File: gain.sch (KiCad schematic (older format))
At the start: 15 parts

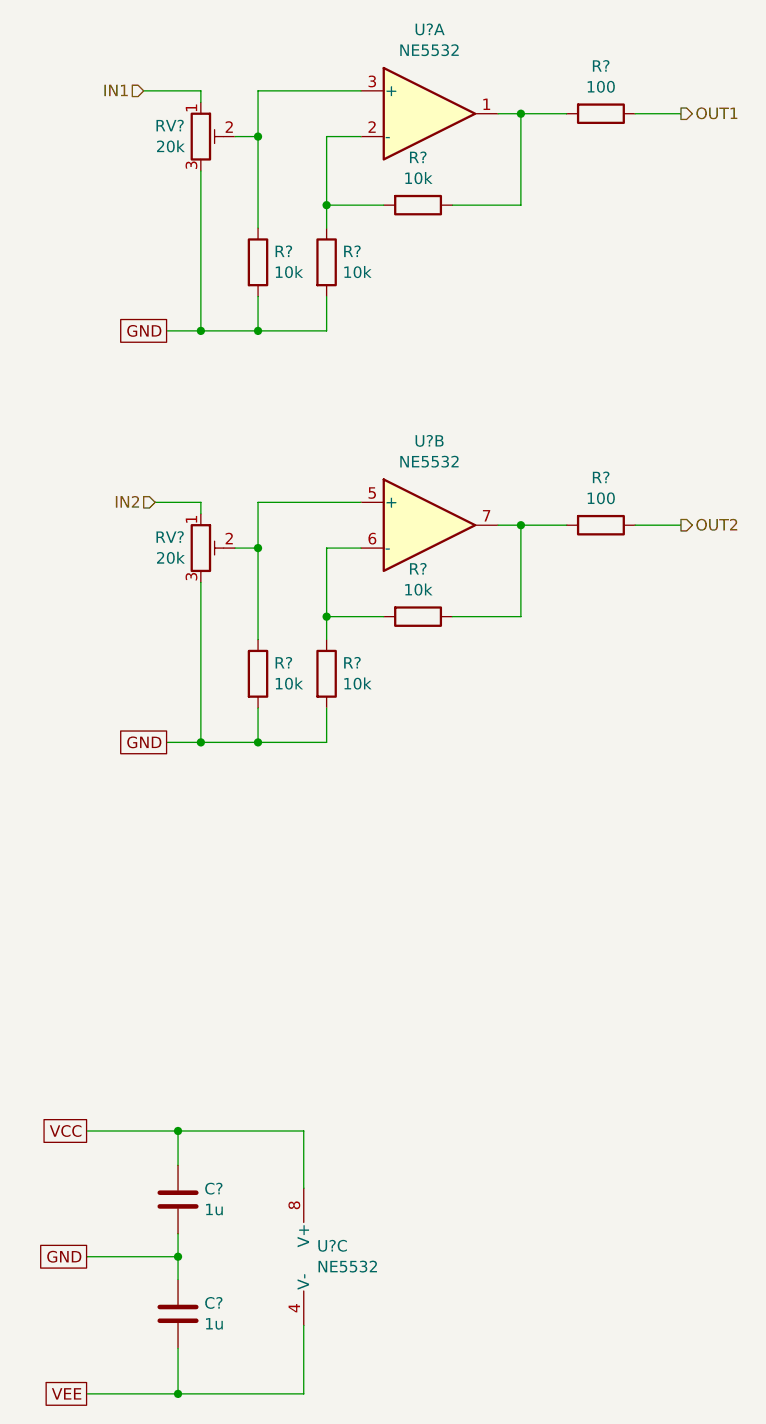
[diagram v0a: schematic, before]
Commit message: improved PSU, gain up front, reordered filter stages, shrunk rumble filter
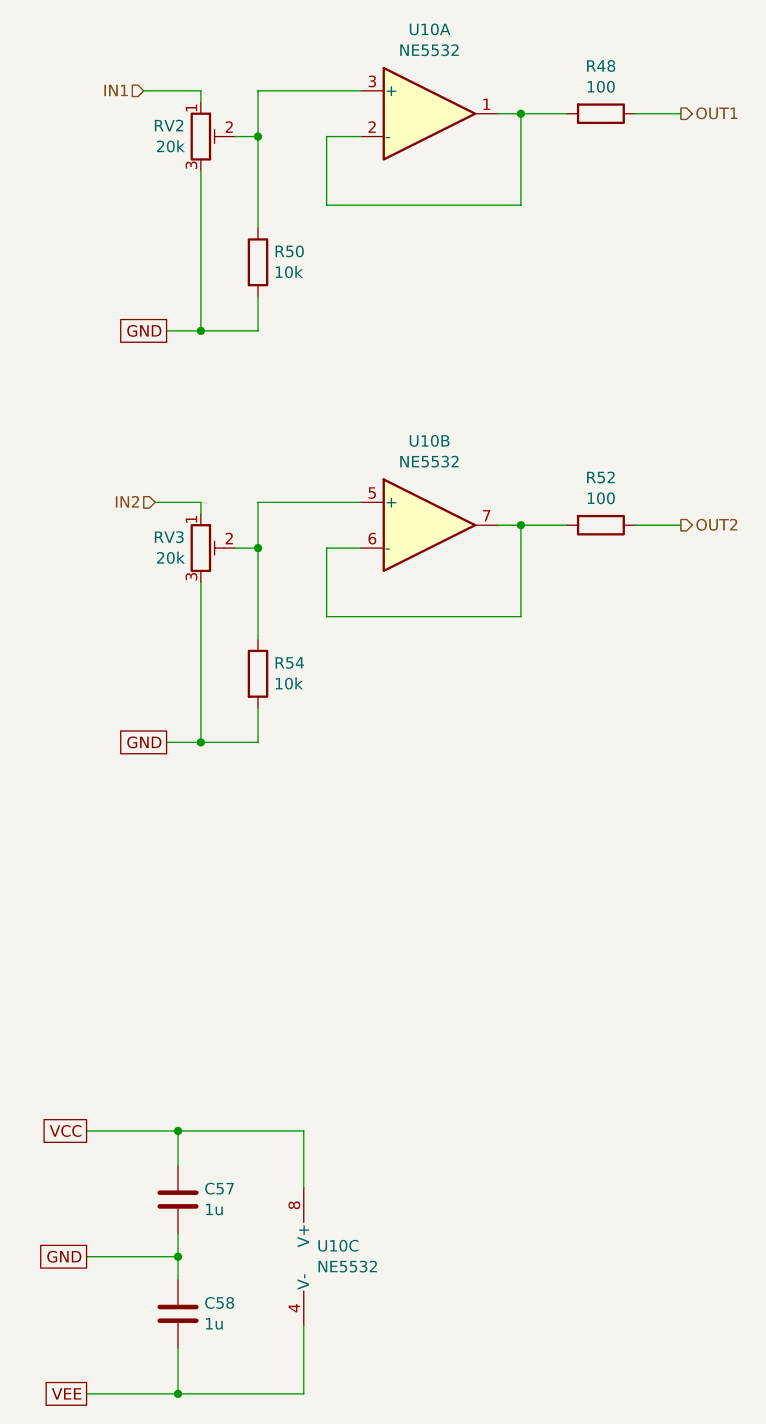
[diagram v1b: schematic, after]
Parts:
- removed R? (x4): 10k, Resistors_SMD:R_0805, symbol Device:R
- gave numbers to parts that had none: 9
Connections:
- net at R56.2, U11.1: now also U11.2 (-)
- net at U11.6 (-): now also R60.2, U11.7
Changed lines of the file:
@@
 $Descr A4 11693 8268
 encoding utf-8
-Sheet 11 13
+Sheet 13 13
 Title "Output Gain Controls"
 Date "2021-10-03"
@@
 AR Path="/61597701/61606DFA" Ref="U?"  Part="3"
 AR Path="/615C4B54/61606DFA" Ref="U?"  Part="3"
-AR Path="/61604458/61606DFA" Ref="U?"  Part="3"
-AR Path="/6164D7C0/61606DFA" Ref="U?"  Part="3"
+AR Path="/61604458/61606DFA" Ref="U11"  Part="3"
+AR Path="/6164D7C0/61606DFA" Ref="U10"  Part="3"
 AR Path="/61651AA2/61606DFA" Ref="U?"  Part="3"
-F 0 "U?" H 2808 6846 50  0000 L CNN
+F 0 "U10" H 2808 6846 50  0000 L CNN
 F 1 "NE5532" H 2808 6755 50  0000 L CNN
 F 2 "Housings_DIP:DIP-8_W7.62mm_Socket" H 2850 6800 50  0001 C CNN
@@
 AR Path="/61597701/61606E00" Ref="C?"  Part="1"
 AR Path="/615C4B54/61606E00" Ref="C?"  Part="1"
-AR Path="/61604458/61606E00" Ref="C?"  Part="1"
-AR Path="/6164D7C0/61606E00" Ref="C?"  Part="1"
+AR Path="/61604458/61606E00" Ref="C60"  Part="1"
+AR Path="/6164D7C0/61606E00" Ref="C58"  Part="1"
 AR Path="/61651AA2/61606E00" Ref="C?"  Part="1"
-F 0 "C?" H 2315 7096 50  0000 L CNN
+F 0 "C58" H 2315 7096 50  0000 L CNN
 F 1 "1u" H 2315 7005 50  0000 L CNN
 F 2 "Capacitors_SMD:C_0805" H 2238 6900 50  0001 C CNN
@@
 AR Path="/61597701/61606E06" Ref="C?"  Part="1"
 AR Path="/615C4B54/61606E06" Ref="C?"  Part="1"
-AR Path="/61604458/61606E06" Ref="C?"  Part="1"
-AR Path="/6164D7C0/61606E06" Ref="C?"  Part="1"
+AR Path="/61604458/61606E06" Ref="C59"  Part="1"
+AR Path="/6164D7C0/61606E06" Ref="C57"  Part="1"
 AR Path="/61651AA2/61606E06" Ref="C?"  Part="1"
-F 0 "C?" H 2315 6596 50  0000 L CNN
+F 0 "C57" H 2315 6596 50  0000 L CNN
 F 1 "1u" H 2315 6505 50  0000 L CNN
 F 2 "Capacitors_SMD:C_0805" H 2238 6400 50  0001 C CNN
@@
 Connection ~ 2200 7400
 $Comp
-L Amplifier_Operational:NE5532 U?
+L Amplifier_Operational:NE5532 U11
 U 1 1 6160713F
 P 3300 1800
-AR Path="/61604458/6160713F" Ref="U?"  Part="1"
-AR Path="/6164D7C0/6160713F" Ref="U?"  Part="1"
+AR Path="/61604458/6160713F" Ref="U11"  Part="1"
+AR Path="/6164D7C0/6160713F" Ref="U10"  Part="1"
 AR Path="/61651AA2/6160713F" Ref="U?"  Part="1"
-F 0 "U?" H 3300 2167 50  0000 C CNN
+F 0 "U10" H 3300 2167 50  0000 C CNN
 F 1 "NE5532" H 3300 2076 50  0000 C CNN
 F 2 "" H 3300 1800 50  0001 C CNN
@@
 $EndComp
 $Comp
-L Amplifier_Operational:NE5532 U?
+L Amplifier_Operational:NE5532 U11
 U 2 1 61607B4F
 P 3300 3600
-AR Path="/61604458/61607B4F" Ref="U?"  Part="2"
-AR Path="/6164D7C0/61607B4F" Ref="U?"  Part="2"
+AR Path="/61604458/61607B4F" Ref="U11"  Part="2"
+AR Path="/6164D7C0/61607B4F" Ref="U10"  Part="2"
 AR Path="/61651AA2/61607B4F" Ref="U?"  Part="2"
-F 0 "U?" H 3300 3967 50  0000 C CNN
+F 0 "U10" H 3300 3967 50  0000 C CNN
 F 1 "NE5532" H 3300 3876 50  0000 C CNN
 F 2 "" H 3300 3600 50  0001 C CNN
@@
 $EndComp
 $Comp
-L Device:R_POT_TRIM RV?
+L Device:R_POT_TRIM RV4
 U 1 1 6160B080
 P 2300 1900
-AR Path="/61604458/6160B080" Ref="RV?"  Part="1"
-AR Path="/6164D7C0/6160B080" Ref="RV?"  Part="1"
+AR Path="/61604458/6160B080" Ref="RV4"  Part="1"
+AR Path="/6164D7C0/6160B080" Ref="RV2"  Part="1"
 AR Path="/61651AA2/6160B080" Ref="RV?"  Part="1"
-F 0 "RV?" H 2230 1946 50  0000 R CNN
+F 0 "RV2" H 2230 1946 50  0000 R CNN
 F 1 "20k" H 2230 1855 50  0000 R CNN
 F 2 "Potentiometers:Potentiometer_Trimmer_Bourns_3296W" H 2300 1900 50  0001 C CNN
@@
 $EndComp
 $Comp
-L Device:R R?
+L Device:R R58
 U 1 1 6160B89B
 P 2550 2450
-AR Path="/61604458/6160B89B" Ref="R?"  Part="1"
-AR Path="/6164D7C0/6160B89B" Ref="R?"  Part="1"
+AR Path="/61604458/6160B89B" Ref="R58"  Part="1"
+AR Path="/6164D7C0/6160B89B" Ref="R50"  Part="1"
 AR Path="/61651AA2/6160B89B" Ref="R?"  Part="1"
-F 0 "R?" H 2620 2496 50  0000 L CNN
+F 0 "R50" H 2620 2496 50  0000 L CNN
 F 1 "10k" H 2620 2405 50  0000 L CNN
 F 2 "Resistors_SMD:R_0805" V 2480 2450 50  0001 C CNN
@@
 	1    0    0    -1
 $EndComp
-$Comp
-L Device:R R?
-U 1 1 6160BF26
-P 2850 2450
-AR Path="/61604458/6160BF26" Ref="R?"  Part="1"
-AR Path="/6164D7C0/6160BF26" Ref="R?"  Part="1"
-AR Path="/61651AA2/6160BF26" Ref="R?"  Part="1"
-F 0 "R?" H 2920 2496 50  0000 L CNN
-F 1 "10k" H 2920 2405 50  0000 L CNN
-F 2 "Resistors_SMD:R_0805" V 2780 2450 50  0001 C CNN
-F 3 "~" H 2850 2450 50  0001 C CNN
-	1    2850 2450
-	1    0    0    -1
-$EndComp
-$Comp
-L Device:R R?
-U 1 1 6160C516
-P 3250 2200
-AR Path="/61604458/6160C516" Ref="R?"  Part="1"
-AR Path="/6164D7C0/6160C516" Ref="R?"  Part="1"
-AR Path="/61651AA2/6160C516" Ref="R?"  Part="1"
-F 0 "R?" V 3043 2200 50  0000 C CNN
-F 1 "10k" V 3134 2200 50  0000 C CNN
-F 2 "Resistors_SMD:R_0805" V 3180 2200 50  0001 C CNN
-F 3 "~" H 3250 2200 50  0001 C CNN
-	1    3250 2200
-	0    1    1    0
-$EndComp
 Wire Wire Line
 	2450 1900 2550 1900
@@
 	3000 1900 2850 1900
 Wire Wire Line
-	2850 1900 2850 2200
-Wire Wire Line
-	2850 2200 3100 2200
-Connection ~ 2850 2200
-Wire Wire Line
-	2850 2200 2850 2300
-Wire Wire Line
 	2550 1900 2550 2300
 Wire Wire Line
@@
 	2300 2750 2550 2750
 Wire Wire Line
-	2850 2750 2850 2600
-Wire Wire Line
 	2550 2600 2550 2750
-Wire Wire Line
-	2850 2750 2550 2750
-Connection ~ 2550 2750
 Wire Wire Line
 	2550 1700 3000 1700
@@
 	2300 1700 2300 1750
 $Comp
-L Device:R_POT_TRIM RV?
+L Device:R_POT_TRIM RV5
 U 1 1 61627D7A
 P 2300 3700
-AR Path="/61604458/61627D7A" Ref="RV?"  Part="1"
-AR Path="/6164D7C0/61627D7A" Ref="RV?"  Part="1"
+AR Path="/61604458/61627D7A" Ref="RV5"  Part="1"
+AR Path="/6164D7C0/61627D7A" Ref="RV3"  Part="1"
 AR Path="/61651AA2/61627D7A" Ref="RV?"  Part="1"
-F 0 "RV?" H 2230 3746 50  0000 R CNN
+F 0 "RV3" H 2230 3746 50  0000 R CNN
 F 1 "20k" H 2230 3655 50  0000 R CNN
 F 2 "Potentiometers:Potentiometer_Trimmer_Bourns_3296W" H 2300 3700 50  0001 C CNN
@@
 $EndComp
 $Comp
-L Device:R R?
+L Device:R R62
 U 1 1 61627D80
 P 2550 4250
-AR Path="/61604458/61627D80" Ref="R?"  Part="1"
-AR Path="/6164D7C0/61627D80" Ref="R?"  Part="1"
+AR Path="/61604458/61627D80" Ref="R62"  Part="1"
+AR Path="/6164D7C0/61627D80" Ref="R54"  Part="1"
 AR Path="/61651AA2/61627D80" Ref="R?"  Part="1"
-F 0 "R?" H 2620 4296 50  0000 L CNN
+F 0 "R54" H 2620 4296 50  0000 L CNN
 F 1 "10k" H 2620 4205 50  0000 L CNN
 F 2 "Resistors_SMD:R_0805" V 2480 4250 50  0001 C CNN
@@
 	1    0    0    -1
 $EndComp
-$Comp
-L Device:R R?
-U 1 1 61627D86
-P 2850 4250
-AR Path="/61604458/61627D86" Ref="R?"  Part="1"
-AR Path="/6164D7C0/61627D86" Ref="R?"  Part="1"
-AR Path="/61651AA2/61627D86" Ref="R?"  Part="1"
-F 0 "R?" H 2920 4296 50  0000 L CNN
-F 1 "10k" H 2920 4205 50  0000 L CNN
-F 2 "Resistors_SMD:R_0805" V 2780 4250 50  0001 C CNN
-F 3 "~" H 2850 4250 50  0001 C CNN
-	1    2850 4250
-	1    0    0    -1
-$EndComp
-$Comp
-L Device:R R?
-U 1 1 61627D8C
-P 3250 4000
-AR Path="/61604458/61627D8C" Ref="R?"  Part="1"
-AR Path="/6164D7C0/61627D8C" Ref="R?"  Part="1"
-AR Path="/61651AA2/61627D8C" Ref="R?"  Part="1"
-F 0 "R?" V 3043 4000 50  0000 C CNN
-F 1 "10k" V 3134 4000 50  0000 C CNN
-F 2 "Resistors_SMD:R_0805" V 3180 4000 50  0001 C CNN
-F 3 "~" H 3250 4000 50  0001 C CNN
-	1    3250 4000
-	0    1    1    0
-$EndComp
-Wire Wire Line
-	2850 3700 2850 4000
-Wire Wire Line
-	2850 4000 3100 4000
-Connection ~ 2850 4000
-Wire Wire Line
-	2850 4000 2850 4100
 Wire Wire Line
 	2550 3700 2550 4100
@@
 	2300 4550 2550 4550
 Wire Wire Line
-	2850 4550 2850 4400
-Wire Wire Line
 	2550 4400 2550 4550
-Wire Wire Line
-	2850 4550 2550 4550
-Connection ~ 2550 4550
 Text GLabel 2150 4550 0    50   UnSpc ~ 0
 GND
@@
 	2550 3500 3000 3500
 Connection ~ 2550 3700
-Wire Wire Line
-	3000 3700 2850 3700
 Text HLabel 2100 3500 0    50   Input ~ 0
 IN2
@@
 Wire Wire Line
 	3700 4000 3700 3600
-Wire Wire Line
-	3400 4000 3700 4000
 Connection ~ 3700 3600
 Wire Wire Line
@@
 Wire Wire Line
 	3700 1800 3900 1800
-Wire Wire Line
-	3400 2200 3700 2200
-$Comp
-L Device:R R?
+$Comp
+L Device:R R56
 U 1 1 61636763
 P 4050 1800
-AR Path="/61604458/61636763" Ref="R?"  Part="1"
-AR Path="/6164D7C0/61636763" Ref="R?"  Part="1"
+AR Path="/61604458/61636763" Ref="R56"  Part="1"
+AR Path="/6164D7C0/61636763" Ref="R48"  Part="1"
 AR Path="/61651AA2/61636763" Ref="R?"  Part="1"
-F 0 "R?" V 3843 1800 50  0000 C CNN
+F 0 "R48" V 3843 1800 50  0000 C CNN
 F 1 "100" V 3934 1800 50  0000 C CNN
 F 2 "Resistors_SMD:R_0805" V 3980 1800 50  0001 C CNN
@@
 	4200 1800 4400 1800
 $Comp
-L Device:R R?
+L Device:R R60
 U 1 1 6163D415
 P 4050 3600
-AR Path="/61604458/6163D415" Ref="R?"  Part="1"
-AR Path="/6164D7C0/6163D415" Ref="R?"  Part="1"
+AR Path="/61604458/6163D415" Ref="R60"  Part="1"
+AR Path="/6164D7C0/6163D415" Ref="R52"  Part="1"
 AR Path="/61651AA2/6163D415" Ref="R?"  Part="1"
-F 0 "R?" V 3843 3600 50  0000 C CNN
+F 0 "R52" V 3843 3600 50  0000 C CNN
 F 1 "100" V 3934 3600 50  0000 C CNN
 F 2 "Resistors_SMD:R_0805" V 3980 3600 50  0001 C CNN
@@
 Wire Wire Line
 	4200 3600 4400 3600
+Wire Wire Line
+	2850 1900 2850 2200
+Wire Wire Line
+	2850 2200 3700 2200
+Wire Wire Line
+	3700 4000 2850 4000
+Wire Wire Line
+	2850 4000 2850 3700
+Wire Wire Line
+	2850 3700 3000 3700
 $EndSCHEMATC

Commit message: added buffered volume pot, and fixed subsonic filter added signal taps for external transforms/filters to be added later
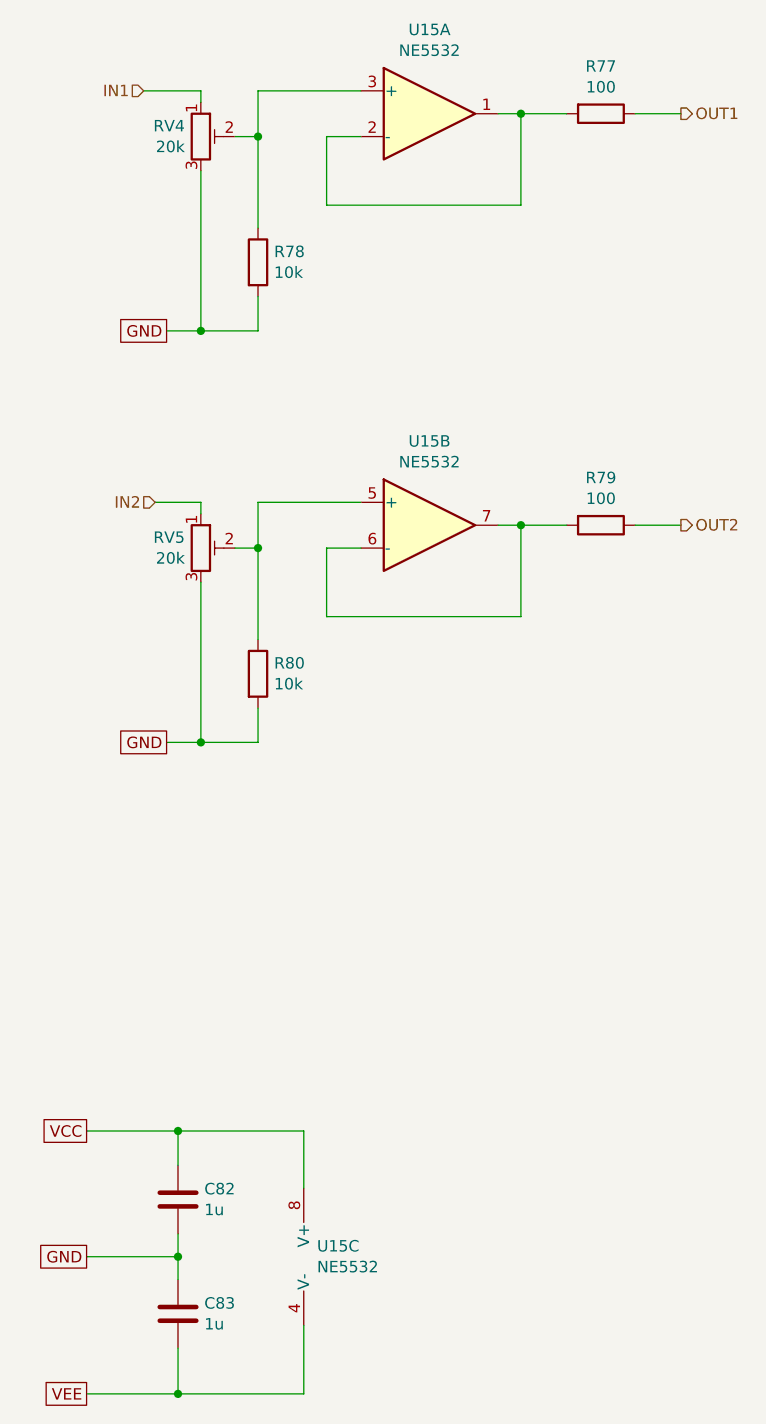
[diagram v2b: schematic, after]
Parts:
- renumbered C59 to C58, C60 to C59, R56 to R53, R58 to R54, R60 to R55, R62 to R56, RV4 to RV2, RV5 to RV3
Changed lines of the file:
@@
 $Descr A4 11693 8268
 encoding utf-8
-Sheet 13 13
+Sheet 13 19
 Title "Output Gain Controls"
 Date "2021-10-03"
@@
 AR Path="/615C4B54/61606DFA" Ref="U?"  Part="3"
 AR Path="/61604458/61606DFA" Ref="U11"  Part="3"
-AR Path="/6164D7C0/61606DFA" Ref="U10"  Part="3"
+AR Path="/6164D7C0/61606DFA" Ref="U15"  Part="3"
 AR Path="/61651AA2/61606DFA" Ref="U?"  Part="3"
-F 0 "U10" H 2808 6846 50  0000 L CNN
+F 0 "U15" H 2808 6846 50  0000 L CNN
 F 1 "NE5532" H 2808 6755 50  0000 L CNN
 F 2 "Housings_DIP:DIP-8_W7.62mm_Socket" H 2850 6800 50  0001 C CNN
@@
 AR Path="/61597701/61606E00" Ref="C?"  Part="1"
 AR Path="/615C4B54/61606E00" Ref="C?"  Part="1"
-AR Path="/61604458/61606E00" Ref="C60"  Part="1"
-AR Path="/6164D7C0/61606E00" Ref="C58"  Part="1"
+AR Path="/61604458/61606E00" Ref="C59"  Part="1"
+AR Path="/6164D7C0/61606E00" Ref="C83"  Part="1"
 AR Path="/61651AA2/61606E00" Ref="C?"  Part="1"
-F 0 "C58" H 2315 7096 50  0000 L CNN
+F 0 "C83" H 2315 7096 50  0000 L CNN
 F 1 "1u" H 2315 7005 50  0000 L CNN
 F 2 "Capacitors_SMD:C_0805" H 2238 6900 50  0001 C CNN
@@
 AR Path="/61597701/61606E06" Ref="C?"  Part="1"
 AR Path="/615C4B54/61606E06" Ref="C?"  Part="1"
-AR Path="/61604458/61606E06" Ref="C59"  Part="1"
-AR Path="/6164D7C0/61606E06" Ref="C57"  Part="1"
+AR Path="/61604458/61606E06" Ref="C58"  Part="1"
+AR Path="/6164D7C0/61606E06" Ref="C82"  Part="1"
 AR Path="/61651AA2/61606E06" Ref="C?"  Part="1"
-F 0 "C57" H 2315 6596 50  0000 L CNN
+F 0 "C82" H 2315 6596 50  0000 L CNN
 F 1 "1u" H 2315 6505 50  0000 L CNN
 F 2 "Capacitors_SMD:C_0805" H 2238 6400 50  0001 C CNN
@@
 P 3300 1800
 AR Path="/61604458/6160713F" Ref="U11"  Part="1"
-AR Path="/6164D7C0/6160713F" Ref="U10"  Part="1"
+AR Path="/6164D7C0/6160713F" Ref="U15"  Part="1"
 AR Path="/61651AA2/6160713F" Ref="U?"  Part="1"
-F 0 "U10" H 3300 2167 50  0000 C CNN
+F 0 "U15" H 3300 2167 50  0000 C CNN
 F 1 "NE5532" H 3300 2076 50  0000 C CNN
 F 2 "" H 3300 1800 50  0001 C CNN
@@
 P 3300 3600
 AR Path="/61604458/61607B4F" Ref="U11"  Part="2"
-AR Path="/6164D7C0/61607B4F" Ref="U10"  Part="2"
+AR Path="/6164D7C0/61607B4F" Ref="U15"  Part="2"
 AR Path="/61651AA2/61607B4F" Ref="U?"  Part="2"
-F 0 "U10" H 3300 3967 50  0000 C CNN
+F 0 "U15" H 3300 3967 50  0000 C CNN
 F 1 "NE5532" H 3300 3876 50  0000 C CNN
 F 2 "" H 3300 3600 50  0001 C CNN
@@
 $EndComp
 $Comp
-L Device:R_POT_TRIM RV4
+L Device:R_POT_TRIM RV2
 U 1 1 6160B080
 P 2300 1900
-AR Path="/61604458/6160B080" Ref="RV4"  Part="1"
-AR Path="/6164D7C0/6160B080" Ref="RV2"  Part="1"
+AR Path="/61604458/6160B080" Ref="RV2"  Part="1"
+AR Path="/6164D7C0/6160B080" Ref="RV4"  Part="1"
 AR Path="/61651AA2/6160B080" Ref="RV?"  Part="1"
-F 0 "RV2" H 2230 1946 50  0000 R CNN
+F 0 "RV4" H 2230 1946 50  0000 R CNN
 F 1 "20k" H 2230 1855 50  0000 R CNN
 F 2 "Potentiometers:Potentiometer_Trimmer_Bourns_3296W" H 2300 1900 50  0001 C CNN
@@
 $EndComp
 $Comp
-L Device:R R58
+L Device:R R54
 U 1 1 6160B89B
 P 2550 2450
-AR Path="/61604458/6160B89B" Ref="R58"  Part="1"
-AR Path="/6164D7C0/6160B89B" Ref="R50"  Part="1"
+AR Path="/61604458/6160B89B" Ref="R54"  Part="1"
+AR Path="/6164D7C0/6160B89B" Ref="R78"  Part="1"
 AR Path="/61651AA2/6160B89B" Ref="R?"  Part="1"
-F 0 "R50" H 2620 2496 50  0000 L CNN
+F 0 "R78" H 2620 2496 50  0000 L CNN
 F 1 "10k" H 2620 2405 50  0000 L CNN
 F 2 "Resistors_SMD:R_0805" V 2480 2450 50  0001 C CNN
@@
 	2300 1700 2300 1750
 $Comp
-L Device:R_POT_TRIM RV5
+L Device:R_POT_TRIM RV3
 U 1 1 61627D7A
 P 2300 3700
-AR Path="/61604458/61627D7A" Ref="RV5"  Part="1"
-AR Path="/6164D7C0/61627D7A" Ref="RV3"  Part="1"
+AR Path="/61604458/61627D7A" Ref="RV3"  Part="1"
+AR Path="/6164D7C0/61627D7A" Ref="RV5"  Part="1"
 AR Path="/61651AA2/61627D7A" Ref="RV?"  Part="1"
-F 0 "RV3" H 2230 3746 50  0000 R CNN
+F 0 "RV5" H 2230 3746 50  0000 R CNN
 F 1 "20k" H 2230 3655 50  0000 R CNN
 F 2 "Potentiometers:Potentiometer_Trimmer_Bourns_3296W" H 2300 3700 50  0001 C CNN
@@
 $EndComp
 $Comp
-L Device:R R62
+L Device:R R56
 U 1 1 61627D80
 P 2550 4250
-AR Path="/61604458/61627D80" Ref="R62"  Part="1"
-AR Path="/6164D7C0/61627D80" Ref="R54"  Part="1"
+AR Path="/61604458/61627D80" Ref="R56"  Part="1"
+AR Path="/6164D7C0/61627D80" Ref="R80"  Part="1"
 AR Path="/61651AA2/61627D80" Ref="R?"  Part="1"
-F 0 "R54" H 2620 4296 50  0000 L CNN
+F 0 "R80" H 2620 4296 50  0000 L CNN
 F 1 "10k" H 2620 4205 50  0000 L CNN
 F 2 "Resistors_SMD:R_0805" V 2480 4250 50  0001 C CNN
@@
 	3700 1800 3900 1800
 $Comp
-L Device:R R56
+L Device:R R53
 U 1 1 61636763
 P 4050 1800
-AR Path="/61604458/61636763" Ref="R56"  Part="1"
-AR Path="/6164D7C0/61636763" Ref="R48"  Part="1"
+AR Path="/61604458/61636763" Ref="R53"  Part="1"
+AR Path="/6164D7C0/61636763" Ref="R77"  Part="1"
 AR Path="/61651AA2/61636763" Ref="R?"  Part="1"
-F 0 "R48" V 3843 1800 50  0000 C CNN
+F 0 "R77" V 3843 1800 50  0000 C CNN
 F 1 "100" V 3934 1800 50  0000 C CNN
 F 2 "Resistors_SMD:R_0805" V 3980 1800 50  0001 C CNN
@@
 	4200 1800 4400 1800
 $Comp
-L Device:R R60
+L Device:R R55
 U 1 1 6163D415
 P 4050 3600
-AR Path="/61604458/6163D415" Ref="R60"  Part="1"
-AR Path="/6164D7C0/6163D415" Ref="R52"  Part="1"
+AR Path="/61604458/6163D415" Ref="R55"  Part="1"
+AR Path="/6164D7C0/6163D415" Ref="R79"  Part="1"
 AR Path="/61651AA2/6163D415" Ref="R?"  Part="1"
-F 0 "R52" V 3843 3600 50  0000 C CNN
+F 0 "R79" V 3843 3600 50  0000 C CNN
 F 1 "100" V 3934 3600 50  0000 C CNN
 F 2 "Resistors_SMD:R_0805" V 3980 3600 50  0001 C CNN
